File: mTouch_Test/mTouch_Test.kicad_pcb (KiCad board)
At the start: 2 copper layers, 91 parts, among them J401 USB_B_Micro, J501 Prog, J601 Barrel_Jack_Switch, Q501 BSS214NW, Q601 Si2319CDS, U201 PIC18LF67K40-I_PT, U301 ISO7331C, U401 74LVC1G17, U402 FT234XD, U403 TPD3S014DBVR, U501 TL331, U502 74LVC1G86, U601 MCP1700-3302E

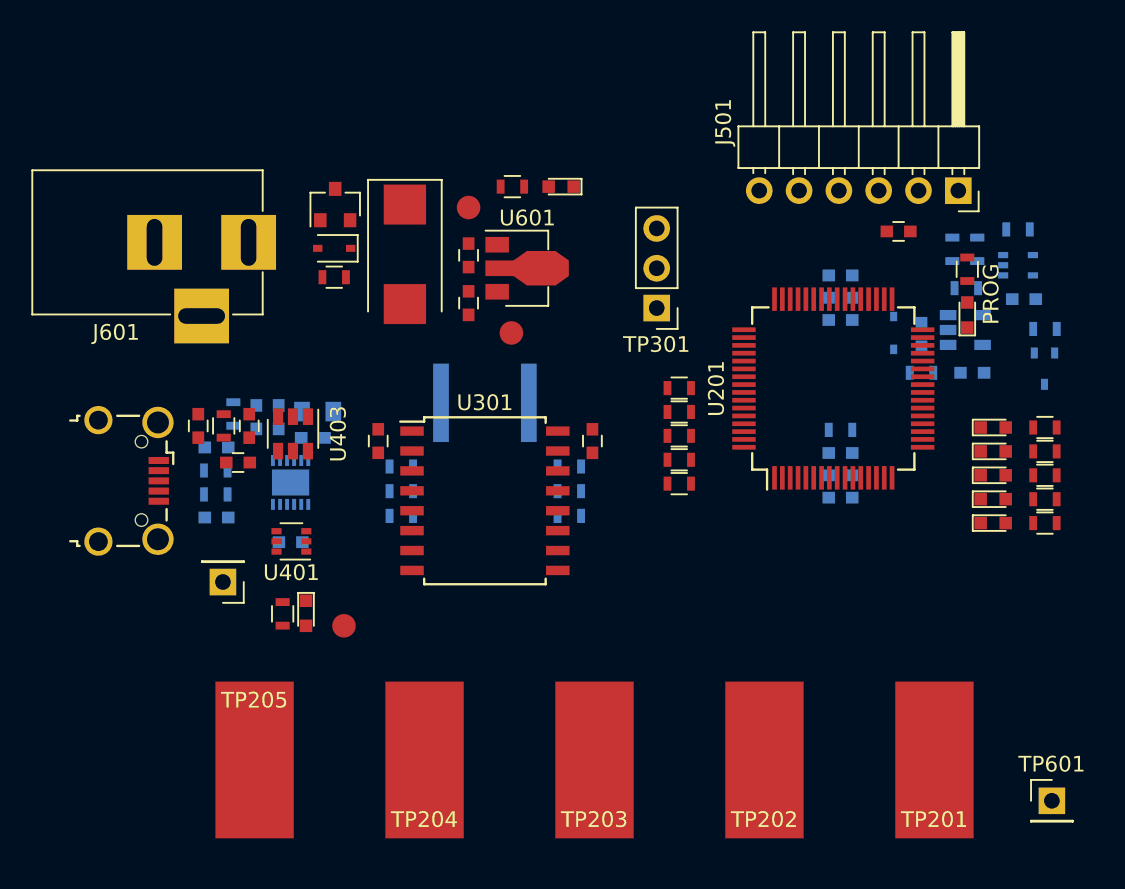
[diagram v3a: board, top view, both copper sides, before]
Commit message: Added board edge
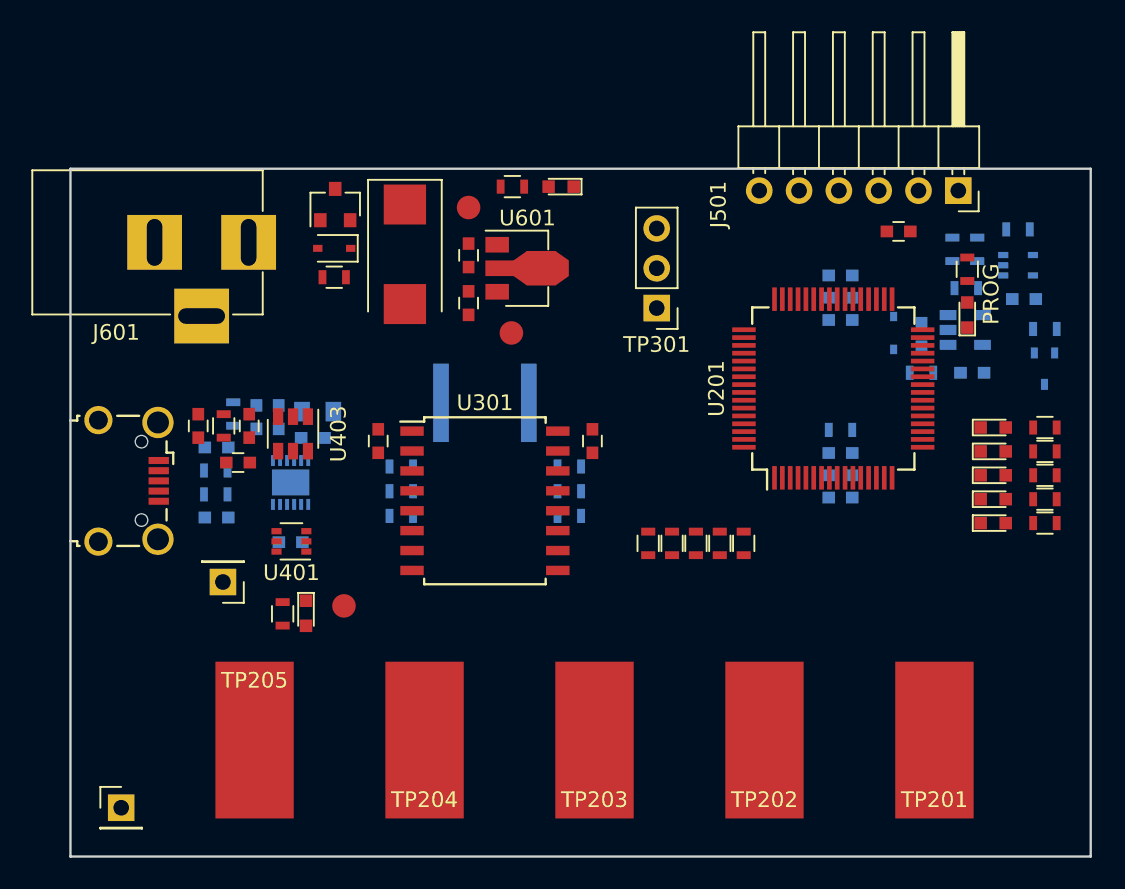
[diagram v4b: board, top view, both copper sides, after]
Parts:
- moved TP601 59.4 mm to (11.7, 145.7)
- moved R206 10.1 mm to (45.4, 128.9), turned to 270 degrees
- moved R205 8.39 mm to (46.9, 128.9), turned to 270 degrees
- moved R204 6.94 mm to (48.4, 128.9), turned to 270 degrees
- moved R203 5.93 mm to (49.9, 128.9), turned to 270 degrees
- moved R202 5.61 mm to (51.5, 128.9), turned to 270 degrees
- moved TP201 1.27 mm to (63.6, 141.4)
- moved TP202 1.27 mm to (52.8, 141.4)
- moved TP203 1.27 mm to (41.9, 141.4)
- moved TP204 1.27 mm to (31.1, 141.4)
- moved TP205 1.27 mm to (20.3, 141.4)
- moved TP401 1.27 mm to (26.0, 132.9)
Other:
- board outline added: 65.1 x 43.9 mm
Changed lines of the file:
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@@
   (general
     (thickness 1.6)
-    (drawings 1)
+    (drawings 6)
     (tracks 0)
     (zones 0)
@@
     (descr "Through hole angled pin header, 1x06, 2.54mm pitch, 6mm pin length, single row")
     (tags "Through hole angled pin header THT 1x06 2.54mm single row")
-    (fp_text reference J501 (at 4.385 -2.27 90) (layer F.SilkS)
+    (fp_text reference J501 (at -0.889 -2.6035 90) (layer F.SilkS)
       (effects (font (size 1 1) (thickness 0.15)))
     )
@@
   )
   (module Resistors_SMD:R_0603 (layer F.Cu)
-    (at 47.3456 125.0569 180)
+    (at 51.4604 128.8669 270)
     (descr "Resistor SMD 0603, reflow soldering, Vishay (see dcrcw.pdf)")
     (tags "resistor 0603")
     (attr smd)
-    (fp_text reference R202 (at 0 -1.45 180) (layer F.SilkS) hide
+    (fp_text reference R202 (at 0 -1.45 270) (layer F.SilkS) hide
       (effects (font (size 1 1) (thickness 0.15)))
     )
-    (fp_text value 220 (at 0 1.5 180) (layer F.Fab)
+    (fp_text value 220 (at 0 1.5 270) (layer F.Fab)
       (effects (font (size 1 1) (thickness 0.15)))
     )
@@
     (fp_line (start 0.8 0.4) (end -0.8 0.4) (layer F.Fab) (width 0.1))
     (fp_line (start -0.8 0.4) (end -0.8 -0.4) (layer F.Fab) (width 0.1))
-    (fp_text user %R (at 0 0 180) (layer F.Fab)
+    (fp_text user %R (at 0 0 270) (layer F.Fab)
       (effects (font (size 0.4 0.4) (thickness 0.075)))
     )
-    (pad 2 smd rect (at 0.75 0 180) (size 0.5 0.9) (layers F.Cu F.Paste F.Mask)
+    (pad 2 smd rect (at 0.75 0 270) (size 0.5 0.9) (layers F.Cu F.Paste F.Mask)
       (net 38 "Net-(R202-Pad2)"))
-    (pad 1 smd rect (at -0.75 0 180) (size 0.5 0.9) (layers F.Cu F.Paste F.Mask)
+    (pad 1 smd rect (at -0.75 0 270) (size 0.5 0.9) (layers F.Cu F.Paste F.Mask)
       (net 39 "Net-(R202-Pad1)"))
     (model ${KISYS3DMOD}/Resistors_SMD.3dshapes/R_0603.wrl
@@
   )
   (module Resistors_SMD:R_0603 (layer F.Cu)
-    (at 47.3456 123.5329 180)
+    (at 49.9364 128.8669 270)
     (descr "Resistor SMD 0603, reflow soldering, Vishay (see dcrcw.pdf)")
     (tags "resistor 0603")
     (attr smd)
-    (fp_text reference R203 (at 0 -1.45 180) (layer F.SilkS) hide
+    (fp_text reference R203 (at 0 -1.45 270) (layer F.SilkS) hide
       (effects (font (size 1 1) (thickness 0.15)))
     )
-    (fp_text value 220 (at 0 1.5 180) (layer F.Fab)
+    (fp_text value 220 (at 0 1.5 270) (layer F.Fab)
       (effects (font (size 1 1) (thickness 0.15)))
     )
-    (fp_text user %R (at 0 0 180) (layer F.Fab)
+    (fp_text user %R (at 0 0 270) (layer F.Fab)
       (effects (font (size 0.4 0.4) (thickness 0.075)))
     )
@@
     (fp_line (start 1.25 0.7) (end 1.25 -0.7) (layer F.CrtYd) (width 0.05))
     (fp_line (start 1.25 0.7) (end -1.25 0.7) (layer F.CrtYd) (width 0.05))
-    (pad 1 smd rect (at -0.75 0 180) (size 0.5 0.9) (layers F.Cu F.Paste F.Mask)
+    (pad 1 smd rect (at -0.75 0 270) (size 0.5 0.9) (layers F.Cu F.Paste F.Mask)
       (net 40 "Net-(R203-Pad1)"))
-    (pad 2 smd rect (at 0.75 0 180) (size 0.5 0.9) (layers F.Cu F.Paste F.Mask)
+    (pad 2 smd rect (at 0.75 0 270) (size 0.5 0.9) (layers F.Cu F.Paste F.Mask)
       (net 41 "Net-(R203-Pad2)"))
     (model ${KISYS3DMOD}/Resistors_SMD.3dshapes/R_0603.wrl
@@
   )
   (module Resistors_SMD:R_0603 (layer F.Cu)
-    (at 47.3456 122.0089 180)
+    (at 48.4124 128.8669 270)
     (descr "Resistor SMD 0603, reflow soldering, Vishay (see dcrcw.pdf)")
     (tags "resistor 0603")
     (attr smd)
-    (fp_text reference R204 (at 0 -1.45 180) (layer F.SilkS) hide
+    (fp_text reference R204 (at 0 -1.45 270) (layer F.SilkS) hide
       (effects (font (size 1 1) (thickness 0.15)))
     )
-    (fp_text value 220 (at 0 1.5 180) (layer F.Fab)
+    (fp_text value 220 (at 0 1.5 270) (layer F.Fab)
       (effects (font (size 1 1) (thickness 0.15)))
     )
@@
     (fp_line (start 0.8 0.4) (end -0.8 0.4) (layer F.Fab) (width 0.1))
     (fp_line (start -0.8 0.4) (end -0.8 -0.4) (layer F.Fab) (width 0.1))
-    (fp_text user %R (at 0 0 180) (layer F.Fab)
+    (fp_text user %R (at 0 0 270) (layer F.Fab)
       (effects (font (size 0.4 0.4) (thickness 0.075)))
     )
-    (pad 2 smd rect (at 0.75 0 180) (size 0.5 0.9) (layers F.Cu F.Paste F.Mask)
+    (pad 2 smd rect (at 0.75 0 270) (size 0.5 0.9) (layers F.Cu F.Paste F.Mask)
       (net 42 "Net-(R204-Pad2)"))
-    (pad 1 smd rect (at -0.75 0 180) (size 0.5 0.9) (layers F.Cu F.Paste F.Mask)
+    (pad 1 smd rect (at -0.75 0 270) (size 0.5 0.9) (layers F.Cu F.Paste F.Mask)
       (net 43 "Net-(R204-Pad1)"))
     (model ${KISYS3DMOD}/Resistors_SMD.3dshapes/R_0603.wrl
@@
   )
   (module Resistors_SMD:R_0603 (layer F.Cu)
-    (at 47.3456 120.4849 180)
+    (at 46.8884 128.8669 270)
     (descr "Resistor SMD 0603, reflow soldering, Vishay (see dcrcw.pdf)")
     (tags "resistor 0603")
     (attr smd)
-    (fp_text reference R205 (at 0 -1.45 180) (layer F.SilkS) hide
+    (fp_text reference R205 (at 0 -1.45 270) (layer F.SilkS) hide
       (effects (font (size 1 1) (thickness 0.15)))
     )
-    (fp_text value 220 (at 0 1.5 180) (layer F.Fab)
+    (fp_text value 220 (at 0 1.5 270) (layer F.Fab)
       (effects (font (size 1 1) (thickness 0.15)))
     )
-    (fp_text user %R (at 0 0 180) (layer F.Fab)
+    (fp_text user %R (at 0 0 270) (layer F.Fab)
       (effects (font (size 0.4 0.4) (thickness 0.075)))
     )
@@
     (fp_line (start 1.25 0.7) (end 1.25 -0.7) (layer F.CrtYd) (width 0.05))
     (fp_line (start 1.25 0.7) (end -1.25 0.7) (layer F.CrtYd) (width 0.05))
-    (pad 1 smd rect (at -0.75 0 180) (size 0.5 0.9) (layers F.Cu F.Paste F.Mask)
+    (pad 1 smd rect (at -0.75 0 270) (size 0.5 0.9) (layers F.Cu F.Paste F.Mask)
       (net 44 "Net-(R205-Pad1)"))
-    (pad 2 smd rect (at 0.75 0 180) (size 0.5 0.9) (layers F.Cu F.Paste F.Mask)
+    (pad 2 smd rect (at 0.75 0 270) (size 0.5 0.9) (layers F.Cu F.Paste F.Mask)
       (net 45 "Net-(R205-Pad2)"))
     (model ${KISYS3DMOD}/Resistors_SMD.3dshapes/R_0603.wrl
@@
   )
   (module Resistors_SMD:R_0603 (layer F.Cu)
-    (at 47.3456 118.9609 180)
+    (at 45.3644 128.8669 270)
     (descr "Resistor SMD 0603, reflow soldering, Vishay (see dcrcw.pdf)")
     (tags "resistor 0603")
     (attr smd)
-    (fp_text reference R206 (at 0 -1.45 180) (layer F.SilkS) hide
+    (fp_text reference R206 (at 0 -1.45 270) (layer F.SilkS) hide
       (effects (font (size 1 1) (thickness 0.15)))
     )
-    (fp_text value 220 (at 0 1.5 180) (layer F.Fab)
+    (fp_text value 220 (at 0 1.5 270) (layer F.Fab)
       (effects (font (size 1 1) (thickness 0.15)))
     )
@@
     (fp_line (start 0.8 0.4) (end -0.8 0.4) (layer F.Fab) (width 0.1))
     (fp_line (start -0.8 0.4) (end -0.8 -0.4) (layer F.Fab) (width 0.1))
-    (fp_text user %R (at 0 0 180) (layer F.Fab)
+    (fp_text user %R (at 0 0 270) (layer F.Fab)
       (effects (font (size 0.4 0.4) (thickness 0.075)))
     )
-    (pad 2 smd rect (at 0.75 0 180) (size 0.5 0.9) (layers F.Cu F.Paste F.Mask)
+    (pad 2 smd rect (at 0.75 0 270) (size 0.5 0.9) (layers F.Cu F.Paste F.Mask)
       (net 46 "Net-(R206-Pad2)"))
-    (pad 1 smd rect (at -0.75 0 180) (size 0.5 0.9) (layers F.Cu F.Paste F.Mask)
+    (pad 1 smd rect (at -0.75 0 270) (size 0.5 0.9) (layers F.Cu F.Paste F.Mask)
       (net 47 "Net-(R206-Pad1)"))
     (model ${KISYS3DMOD}/Resistors_SMD.3dshapes/R_0603.wrl
@@
   )
   (module Wire_Pads:SolderWirePad_single_SMD_5x10mm (layer F.Cu)
-    (at 63.627 142.6845 180)
+    (at 63.627 141.4145 180)
     (descr "Wire Pad, Square, SMD Pad,  5mm x 10mm,")
     (tags "MesurementPoint Square SMDPad 5mmx10mm ")
@@
   )
   (module Wire_Pads:SolderWirePad_single_SMD_5x10mm (layer F.Cu)
-    (at 52.784375 142.6845 180)
+    (at 52.784375 141.4145 180)
     (descr "Wire Pad, Square, SMD Pad,  5mm x 10mm,")
     (tags "MesurementPoint Square SMDPad 5mmx10mm ")
@@
   )
   (module Wire_Pads:SolderWirePad_single_SMD_5x10mm (layer F.Cu)
-    (at 41.94175 142.6845 180)
+    (at 41.94175 141.4145 180)
     (descr "Wire Pad, Square, SMD Pad,  5mm x 10mm,")
     (tags "MesurementPoint Square SMDPad 5mmx10mm ")
@@
   )
   (module Wire_Pads:SolderWirePad_single_SMD_5x10mm (layer F.Cu)
-    (at 31.099125 142.6845 180)
+    (at 31.099125 141.4145 180)
     (descr "Wire Pad, Square, SMD Pad,  5mm x 10mm,")
     (tags "MesurementPoint Square SMDPad 5mmx10mm ")
@@
   )
   (module Wire_Pads:SolderWirePad_single_SMD_5x10mm (layer F.Cu)
-    (at 20.2565 142.6845)
+    (at 20.2565 141.4145)
     (descr "Wire Pad, Square, SMD Pad,  5mm x 10mm,")
     (tags "MesurementPoint Square SMDPad 5mmx10mm ")
@@
   )
   (module Measurement_Points:Measurement_Point_Round-SMD-Pad_Small (layer F.Cu)
-    (at 25.9588 134.1247 180)
+    (at 25.9588 132.8547 180)
     (descr "Mesurement Point, Round, SMD Pad, DM 1.5mm,")
     (tags "Mesurement Point Round SMD Pad 1.5mm")
@@
   )
   (module Pin_Headers:Pin_Header_Straight_1x01_Pitch2.54mm (layer F.Cu)
-    (at 71.12 145.288)
+    (at 11.7475 145.7325)
     (descr "Through hole straight pin header, 1x01, 2.54mm pitch, single row")
     (tags "Through hole pin header THT 1x01 2.54mm single row")
-    (fp_text reference TP601 (at 0 -2.33) (layer F.SilkS)
+    (fp_text reference TP601 (at 0 -2.33) (layer F.SilkS) hide
       (effects (font (size 1 1) (thickness 0.15)))
     )
@@
     )
   )
+  (gr_line (start 8.509 148.844) (end 8.509 128.7145) (layer Edge.Cuts) (width 0.15))
+  (gr_line (start 73.5965 148.844) (end 8.509 148.844) (layer Edge.Cuts) (width 0.15))
+  (gr_line (start 73.5965 104.9655) (end 73.5965 148.844) (layer Edge.Cuts) (width 0.15))
+  (gr_line (start 8.509 104.9655) (end 73.5965 104.9655) (layer Edge.Cuts) (width 0.15))
+  (gr_line (start 8.509 128.7145) (end 8.509 104.9655) (layer Edge.Cuts) (width 0.15))
   (gr_text PROG (at 67.2465 112.9665 90) (layer F.SilkS)
     (effects (font (size 1 1) (thickness 0.15)))

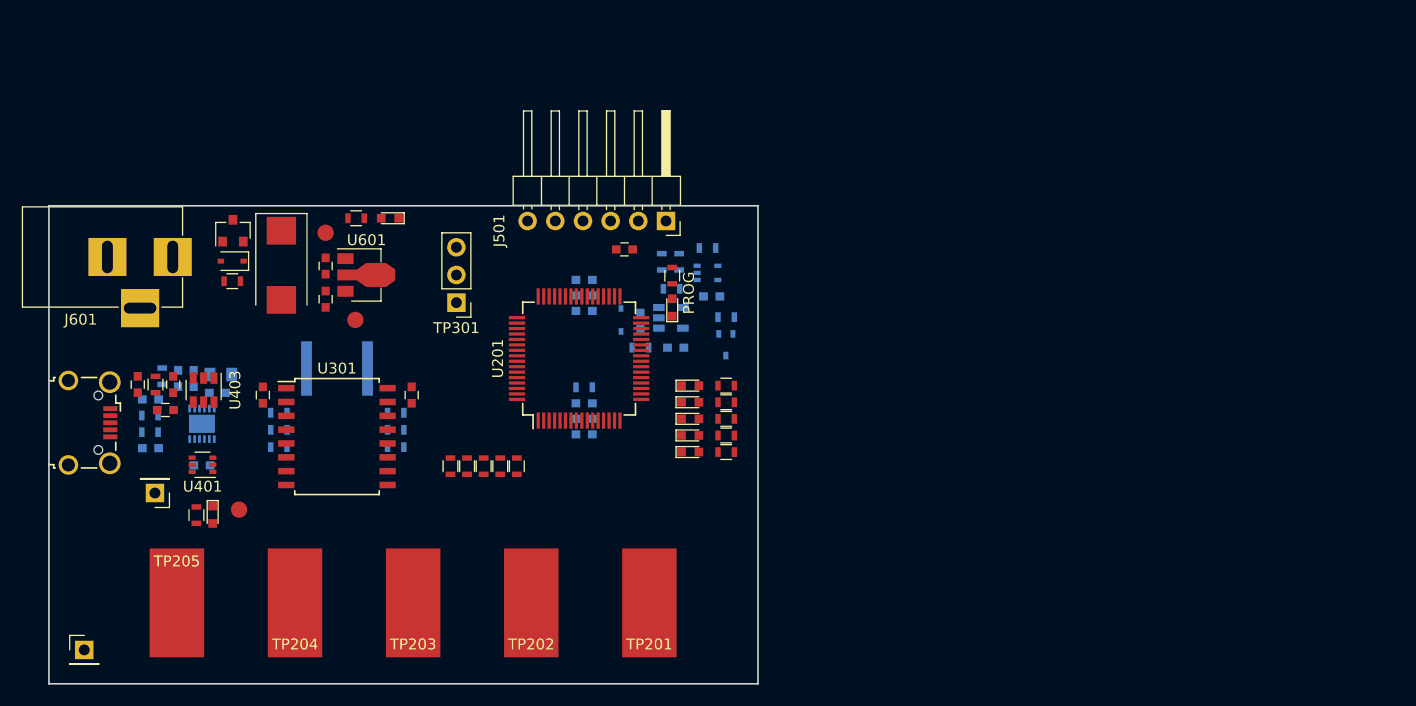
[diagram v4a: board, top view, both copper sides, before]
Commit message: Routed a considerable portion of the board
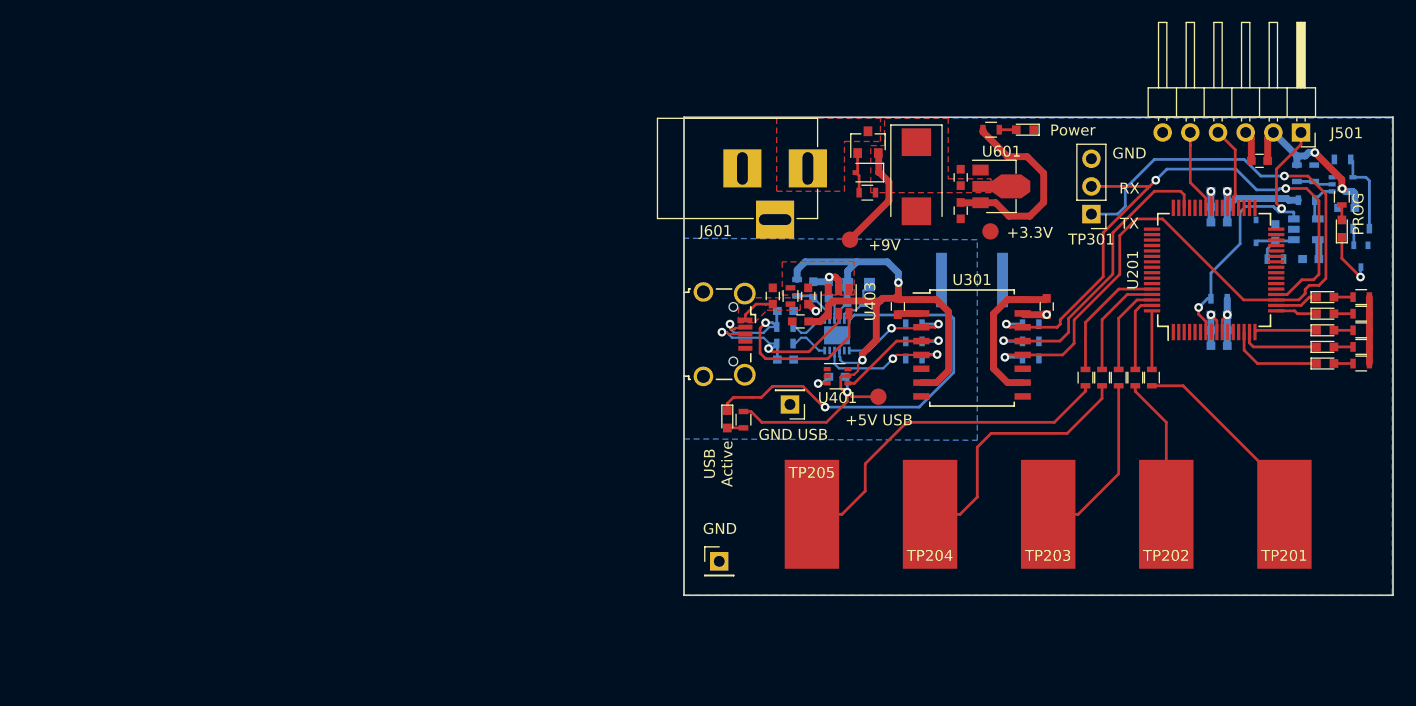
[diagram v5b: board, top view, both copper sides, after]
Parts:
- moved D501 61.9 mm to (127.2, 107.1)
- moved R507 61.9 mm to (127.2, 104.1)
- moved TP401 59.6 mm to (84.6, 122.5)
- moved C402 59.1 mm to (82.5, 113.9)
- moved C403 59.1 mm to (82.8, 112.2)
- moved C201 58.9 mm to (115.9, 103.6)
- moved C202 58.9 mm to (115.9, 105.1)
- moved C203 58.9 mm to (115.9, 106.5)
- moved C204 58.9 mm to (115.9, 115.0)
- moved C205 58.9 mm to (115.9, 116.4)
- moved C206 58.9 mm to (115.9, 117.8)
- moved C404 58.9 mm to (80.1, 112.7)
- moved C405 58.9 mm to (76.1, 119.1)
- moved C406 58.9 mm to (77.5, 115.6)
- moved C407 58.9 mm to (76.1, 114.6)
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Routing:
- net USB_UART_TX: track 0.00 -> 77.5 mm, vias 0 -> 2
- net +5V_USB: track 0.00 -> 72.7 mm, vias 0 -> 3
- net +3V3: track 0.00 -> 71.4 mm, vias 0 -> 4
- net USB_UART_RX: track 0.00 -> 57.2 mm, vias 0 -> 3
- net ~USB_ACTIVE: track 0.00 -> 39.2 mm, vias 0 -> 1
- net Net-(R206-Pad2): track 0.00 -> 31.8 mm
- net USB_DTR: track 0.00 -> 28.4 mm, vias 0 -> 1
- net ~MCLR: track 0.00 -> 28.0 mm, vias 0 -> 2
- net /USB_UART_Converter/CONN_USB-: track 0.00 -> 24.1 mm, vias 0 -> 2
- net Net-(R205-Pad2): track 0.00 -> 24.0 mm
- net /USB_UART_Converter/CONN_USB+: track 0.00 -> 18.6 mm, vias 0 -> 2
- net Net-(R202-Pad2): track 0.00 -> 18.5 mm
- net +9V: track 0.00 -> 17.1 mm
- net Net-(R204-Pad2): track 0.00 -> 16.1 mm
- net GND: track 0.00 -> 14.1 mm, vias 0 -> 3
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- added copper zone on F.Cu, net +9V
- added copper zone on B.Cu, net GND
- added copper zone on F.Cu, net Net-(C408-Pad1)
- added copper zone on F.Cu, net Net-(C409-Pad1)
- added copper zone on F.Cu, net Net-(J601-Pad1)
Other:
- net class Power added: clearance 0.2032, trace_width 0.635, via_dia 0.8, via_drill 0.4
- net class Signal added: clearance 0.2032, trace_width 0.254, via_dia 0.8, via_drill 0.4
- board text added: "+3.3V"
- board text added: "+5V USB"
- board text added: "+9V"
- board text added: "GND"
- board text added: "GND RX TX"
- board text added: "GND USB"
- board text added: "Power"
- board text added: "USB Active"
